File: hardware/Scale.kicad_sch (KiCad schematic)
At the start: 3 parts, among them J1 Load Cell Connector, J4 GPIO, J5 RS232

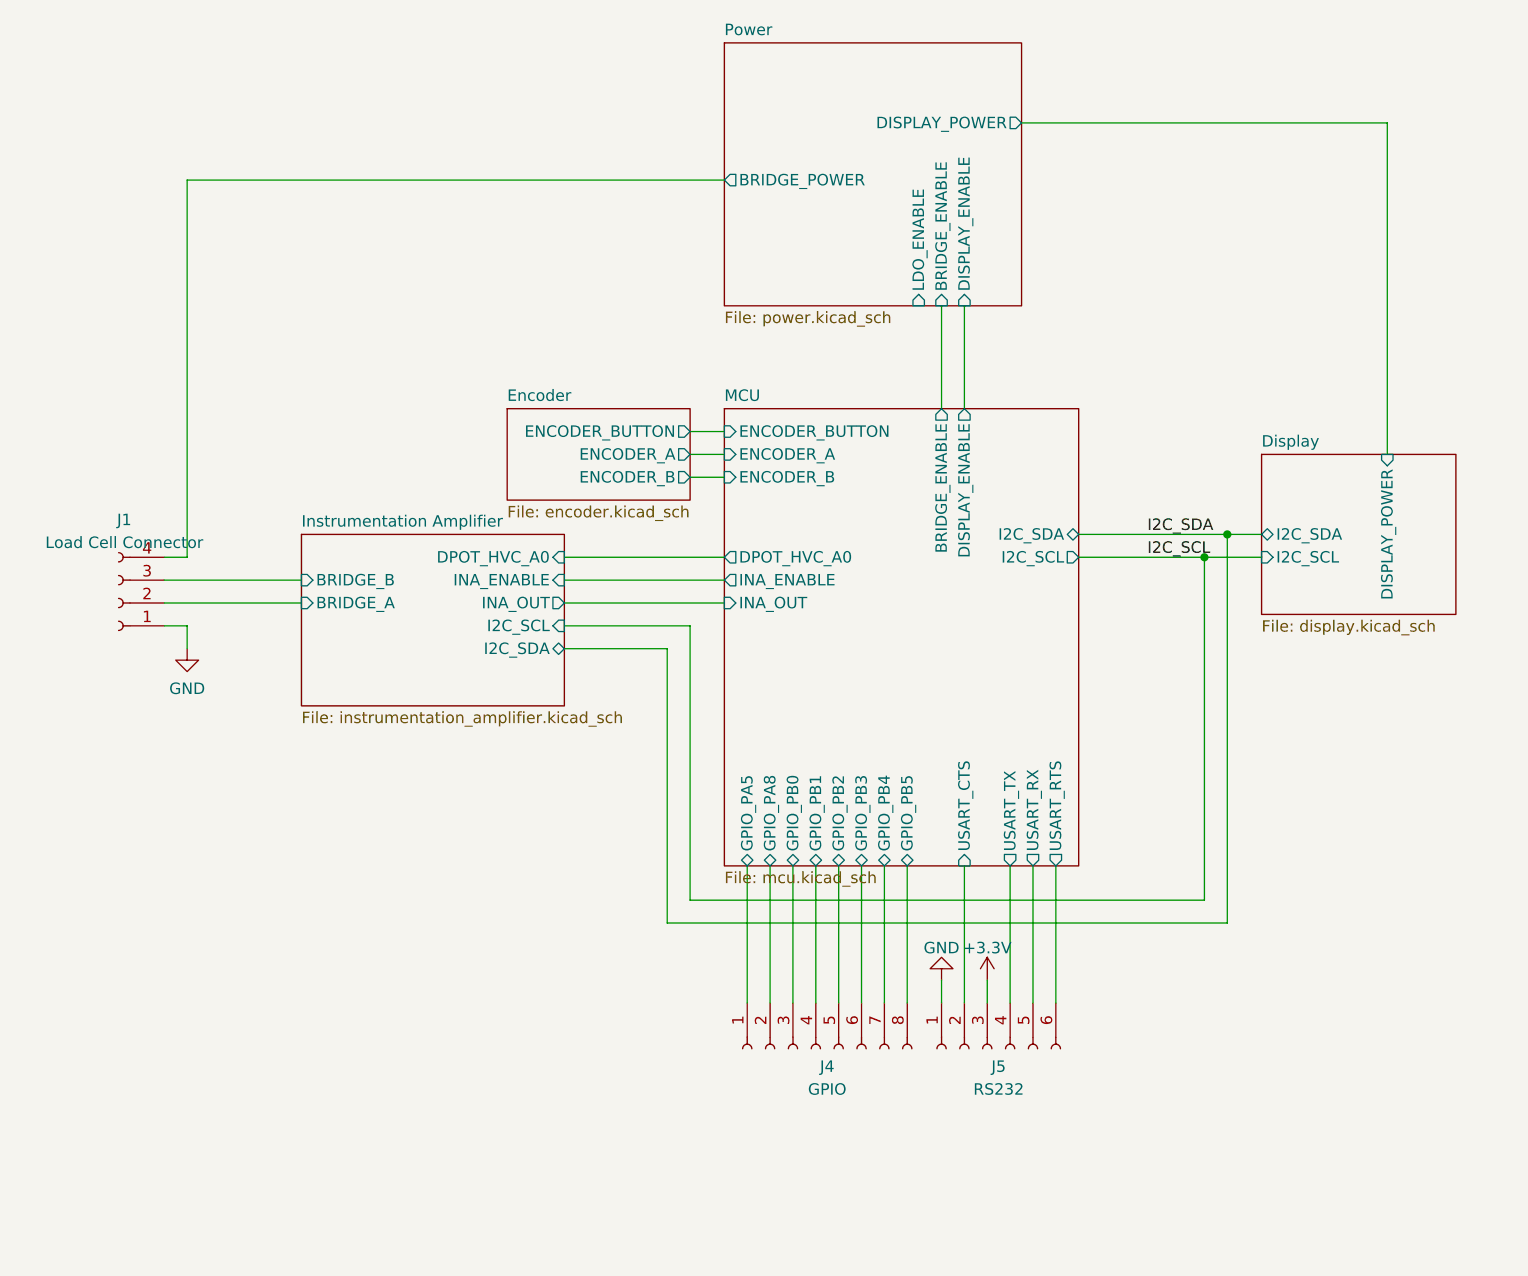
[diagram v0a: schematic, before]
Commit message: Updated schematic according to reference design
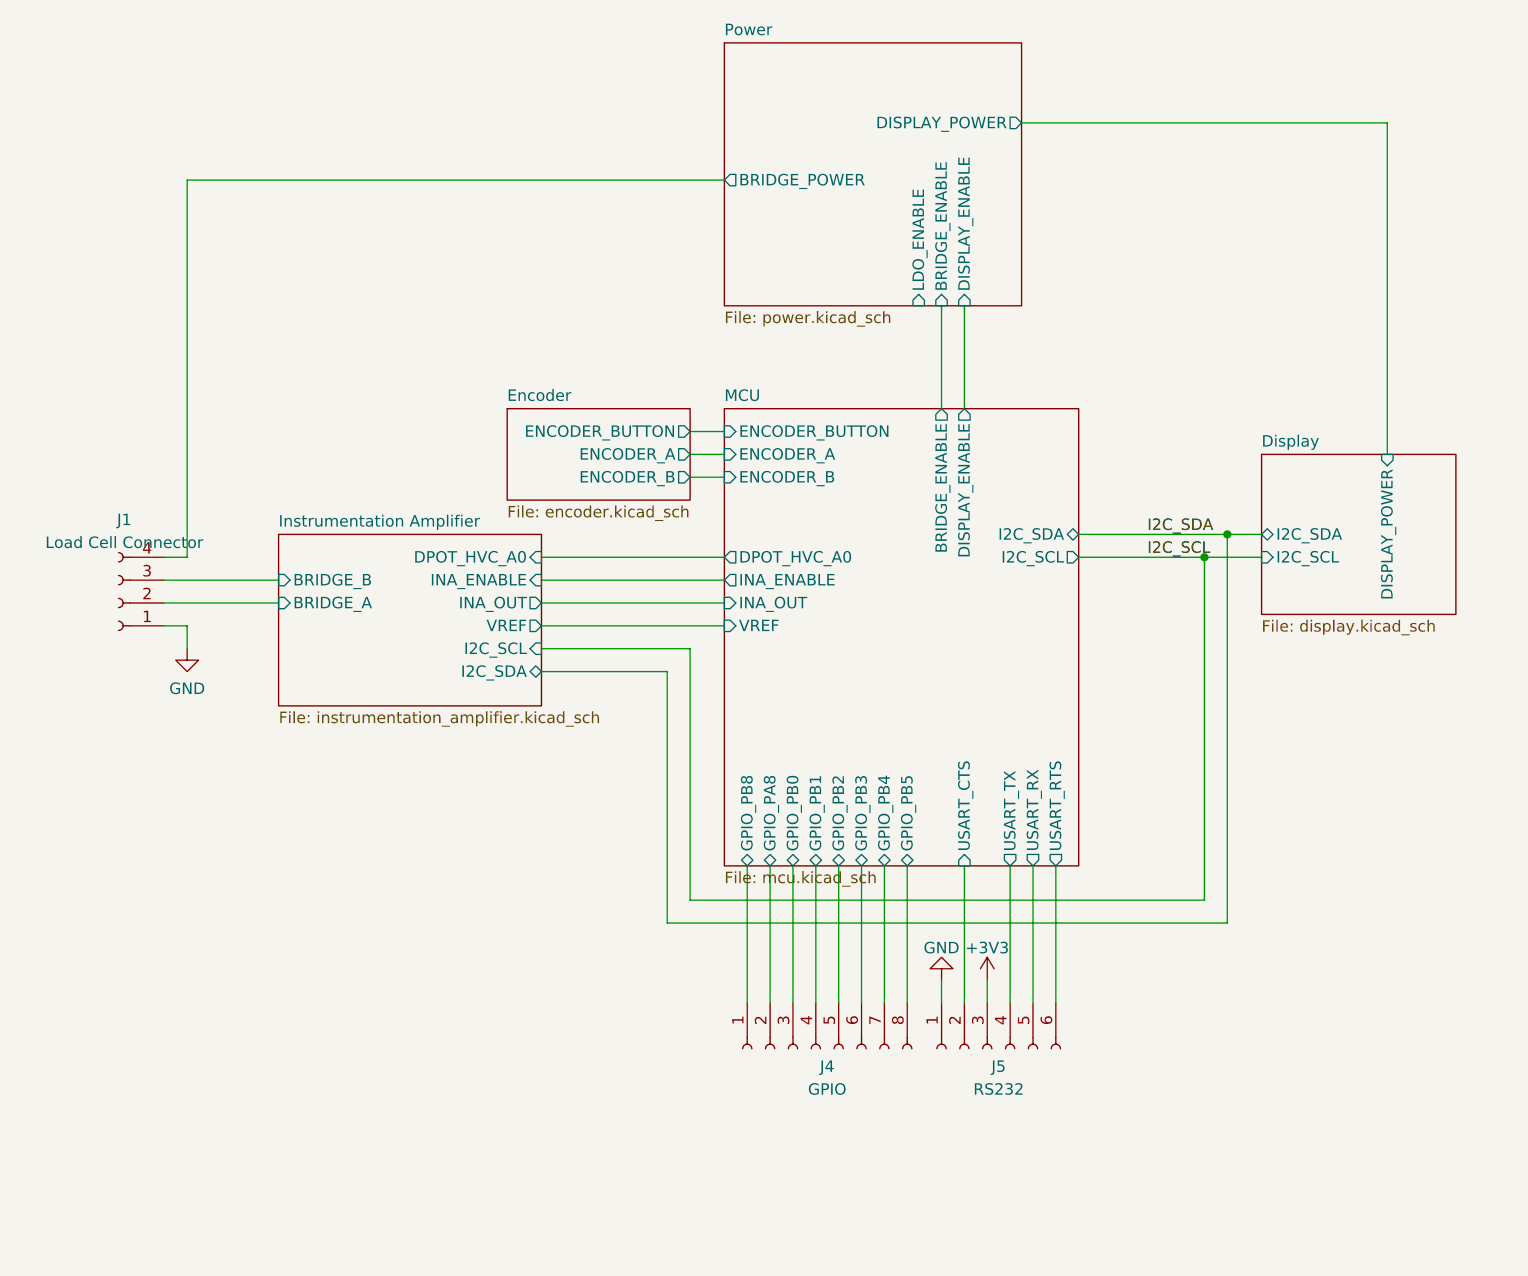
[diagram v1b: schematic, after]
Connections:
- net MCU/GPIO_PA5 renamed MCU/GPIO_PB8
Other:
- sheet Instrumentation Amplifier ports: added VREF; removed none
- sheet MCU ports: added GPIO_PB8, VREF; removed GPIO_PA5

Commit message: Include active filter, ext. ADC, changes to power supply
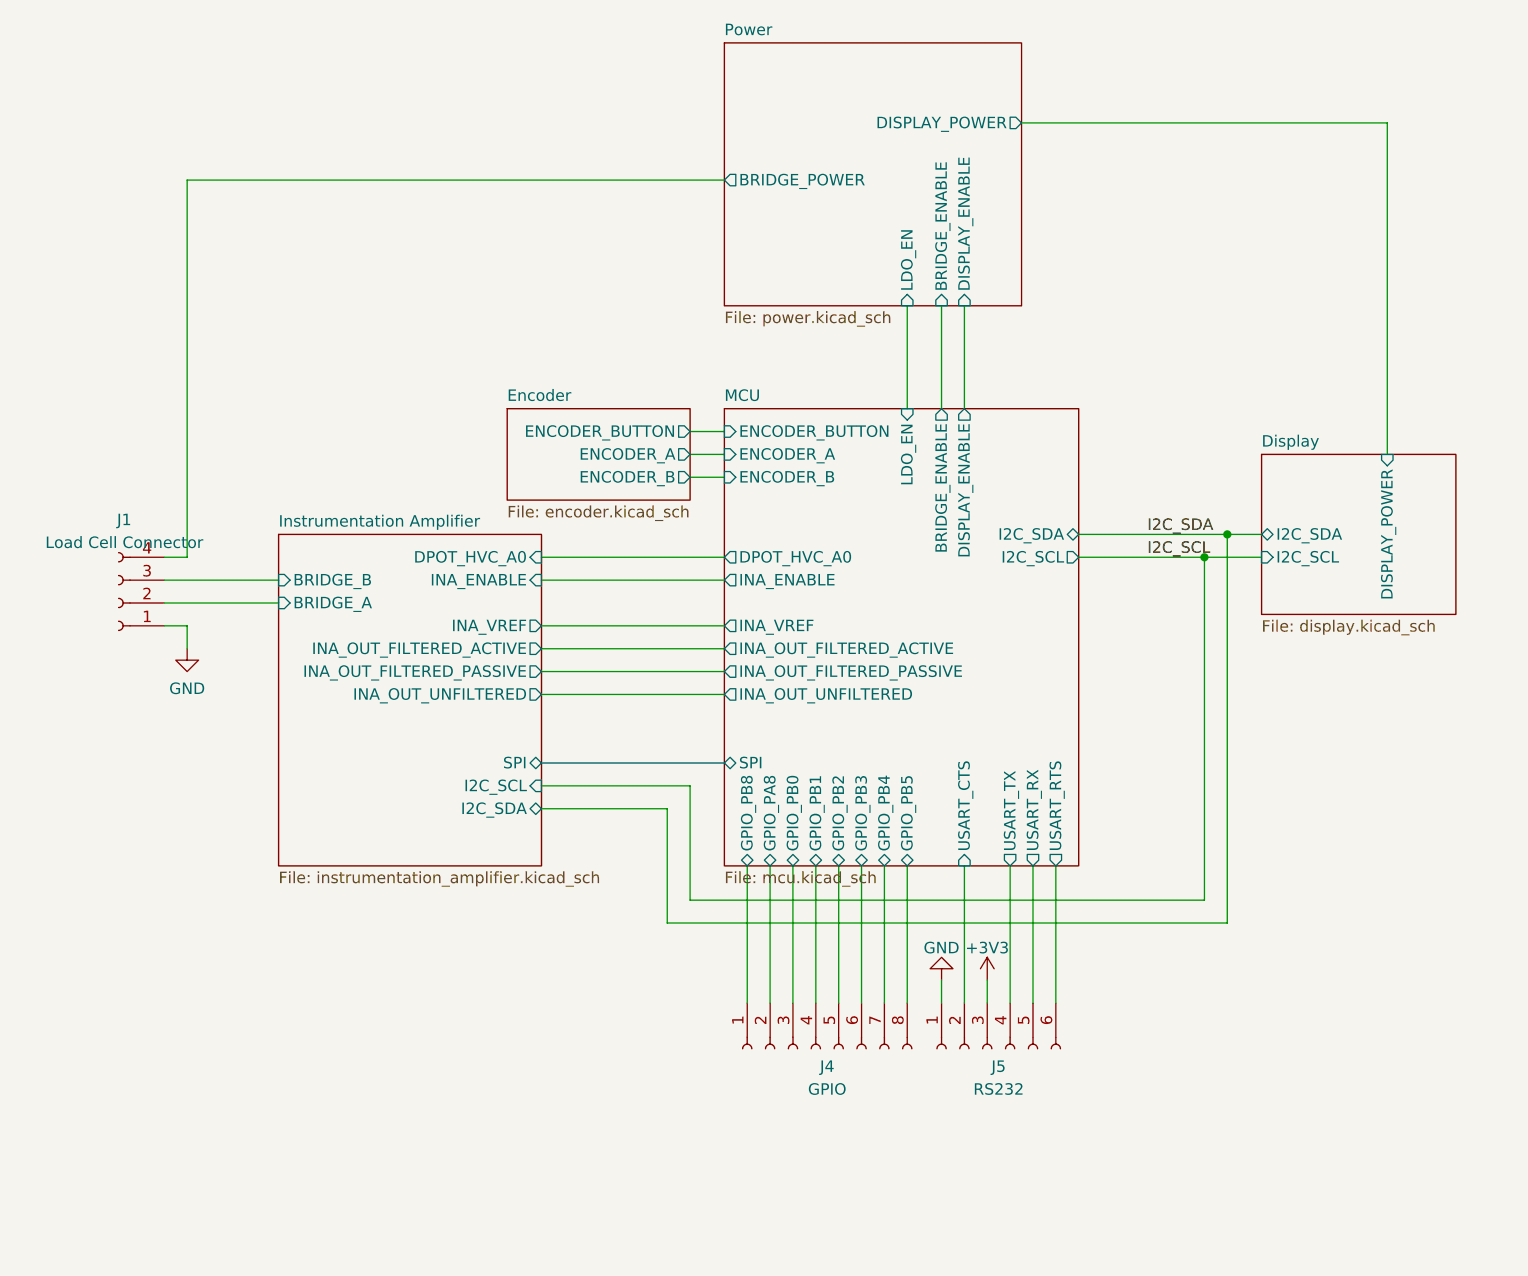
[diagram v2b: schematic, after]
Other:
- sheet Instrumentation Amplifier ports: added INA_OUT_FILTERED_ACTIVE, INA_OUT_FILTERED_PASSIVE, INA_OUT_UNFILTERED, INA_VREF, SPI; removed INA_OUT, VREF
- sheet MCU ports: added INA_OUT_FILTERED_ACTIVE, INA_OUT_FILTERED_PASSIVE, INA_OUT_UNFILTERED, INA_VREF, LDO_EN, SPI; removed INA_OUT, VREF
- sheet Power ports: added LDO_EN; removed LDO_ENABLE
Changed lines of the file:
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@@
-	(wire
-		(pts
-			(xy 99.06 101.6) (xy 119.38 101.6)
-		)
-		(stroke
-			(width 0)
-			(type default)
-		)
-	)
 	(wire
 		(pts
@@
 		)
 	)
+	(bus
+		(pts
+			(xy 99.06 119.38) (xy 119.38 119.38)
+		)
+		(stroke
+			(width 0)
+			(type default)
+		)
+	)
 	(wire
 		(pts
@@
 	(wire
 		(pts
+			(xy 139.7 68.58) (xy 139.7 80.01)
+		)
+		(stroke
+			(width 0)
+			(type default)
+		)
+	)
+	(wire
+		(pts
 			(xy 113.03 137.16) (xy 175.26 137.16)
 		)
@@
 	(wire
 		(pts
-			(xy 99.06 109.22) (xy 113.03 109.22)
+			(xy 99.06 124.46) (xy 113.03 124.46)
+		)
+		(stroke
+			(width 0)
+			(type default)
+		)
+	)
+	(wire
+		(pts
+			(xy 99.06 106.68) (xy 119.38 106.68)
 		)
 		(stroke
@@
 	(wire
 		(pts
+			(xy 99.06 111.76) (xy 119.38 111.76)
+		)
+		(stroke
+			(width 0)
+			(type default)
+		)
+	)
+	(wire
+		(pts
+			(xy 99.06 109.22) (xy 119.38 109.22)
+		)
+		(stroke
+			(width 0)
+			(type default)
+		)
+	)
+	(wire
+		(pts
 			(xy 129.54 130.81) (xy 129.54 146.05)
 		)
@@
 	(wire
 		(pts
-			(xy 113.03 109.22) (xy 113.03 137.16)
+			(xy 113.03 124.46) (xy 113.03 137.16)
 		)
 		(stroke
@@
 	(wire
 		(pts
-			(xy 115.57 106.68) (xy 115.57 134.62)
-		)
-		(stroke
-			(width 0)
-			(type default)
-		)
-	)
-	(wire
-		(pts
-			(xy 99.06 106.68) (xy 115.57 106.68)
+			(xy 115.57 121.92) (xy 115.57 134.62)
+		)
+		(stroke
+			(width 0)
+			(type default)
+		)
+	)
+	(wire
+		(pts
+			(xy 99.06 121.92) (xy 115.57 121.92)
 		)
 		(stroke
@@
 			)
 		)
-		(pin "LDO_ENABLE" input
-			(at 140.97 68.58 270)
+		(pin "LDO_EN" input
+			(at 139.7 68.58 270)
 			(effects
 				(font
@@
 	(sheet
 		(at 69.85 93.98)
-		(size 29.21 19.05)
+		(size 29.21 36.83)
 		(exclude_from_sim no)
 		(in_bom yes)
@@
 		)
 		(property "Sheetfile" "instrumentation_amplifier.kicad_sch"
-			(at 69.85 113.6146 0)
+			(at 69.85 131.3946 0)
 			(effects
 				(font
@@
 				)
 				(justify left top)
-			)
-		)
-		(pin "INA_OUT" output
-			(at 99.06 101.6 0)
-			(effects
-				(font
-					(size 1.27 1.27)
-				)
-				(justify right)
 			)
 		)
@@
 		)
 		(pin "I2C_SCL" input
+			(at 99.06 121.92 0)
+			(effects
+				(font
+					(size 1.27 1.27)
+				)
+				(justify right)
+			)
+		)
+		(pin "I2C_SDA" bidirectional
+			(at 99.06 124.46 0)
+			(effects
+				(font
+					(size 1.27 1.27)
+				)
+				(justify right)
+			)
+		)
+		(pin "SPI" bidirectional
+			(at 99.06 119.38 0)
+			(effects
+				(font
+					(size 1.27 1.27)
+				)
+				(justify right)
+			)
+		)
+		(pin "INA_OUT_FILTERED_ACTIVE" output
 			(at 99.06 106.68 0)
 			(effects
@@
 			)
 		)
-		(pin "I2C_SDA" bidirectional
+		(pin "INA_OUT_FILTERED_PASSIVE" output
 			(at 99.06 109.22 0)
 			(effects
@@
 			)
 		)
-		(pin "VREF" output
+		(pin "INA_OUT_UNFILTERED" output
+			(at 99.06 111.76 0)
+			(effects
+				(font
+					(size 1.27 1.27)
+				)
+				(justify right)
+			)
+		)
+		(pin "INA_VREF" output
 			(at 99.06 104.14 0)
 			(effects
@@
 			)
 		)
-		(pin "INA_OUT" input
-			(at 119.38 101.6 180)
-			(effects
-				(font
-					(size 1.27 1.27)
-				)
-				(justify left)
-			)
-		)
 		(pin "DISPLAY_ENABLE" output
 			(at 146.05 80.01 90)
@@
 			)
 		)
-		(pin "VREF" input
-			(at 119.38 104.14 180)
-			(effects
-				(font
-					(size 1.27 1.27)
-				)
-				(justify left)
-			)
-		)
 		(pin "GPIO_PB8" bidirectional
 			(at 121.92 130.81 270)
@@
 			)
 		)
+		(pin "SPI" bidirectional
+			(at 119.38 119.38 180)
+			(effects
+				(font
+					(size 1.27 1.27)
+				)
+				(justify left)
+			)
+		)
+		(pin "INA_OUT_FILTERED_ACTIVE" output
+			(at 119.38 106.68 180)
+			(effects
+				(font
+					(size 1.27 1.27)
+				)
+				(justify left)
+			)
+		)
+		(pin "INA_OUT_FILTERED_PASSIVE" output
+			(at 119.38 109.22 180)
+			(effects
+				(font
+					(size 1.27 1.27)
+				)
+				(justify left)
+			)
+		)
+		(pin "INA_OUT_UNFILTERED" output
+			(at 119.38 111.76 180)
+			(effects
+				(font
+					(size 1.27 1.27)
+				)
+				(justify left)
+			)
+		)
+		(pin "INA_VREF" output
+			(at 119.38 104.14 180)
+			(effects
+				(font
+					(size 1.27 1.27)
+				)
+				(justify left)
+			)
+		)
+		(pin "LDO_EN" input
+			(at 139.7 80.01 90)
+			(effects
+				(font
+					(size 1.27 1.27)
+				)
+				(justify right)
+			)
+		)

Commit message: Added correct symbol and libraries for ADC
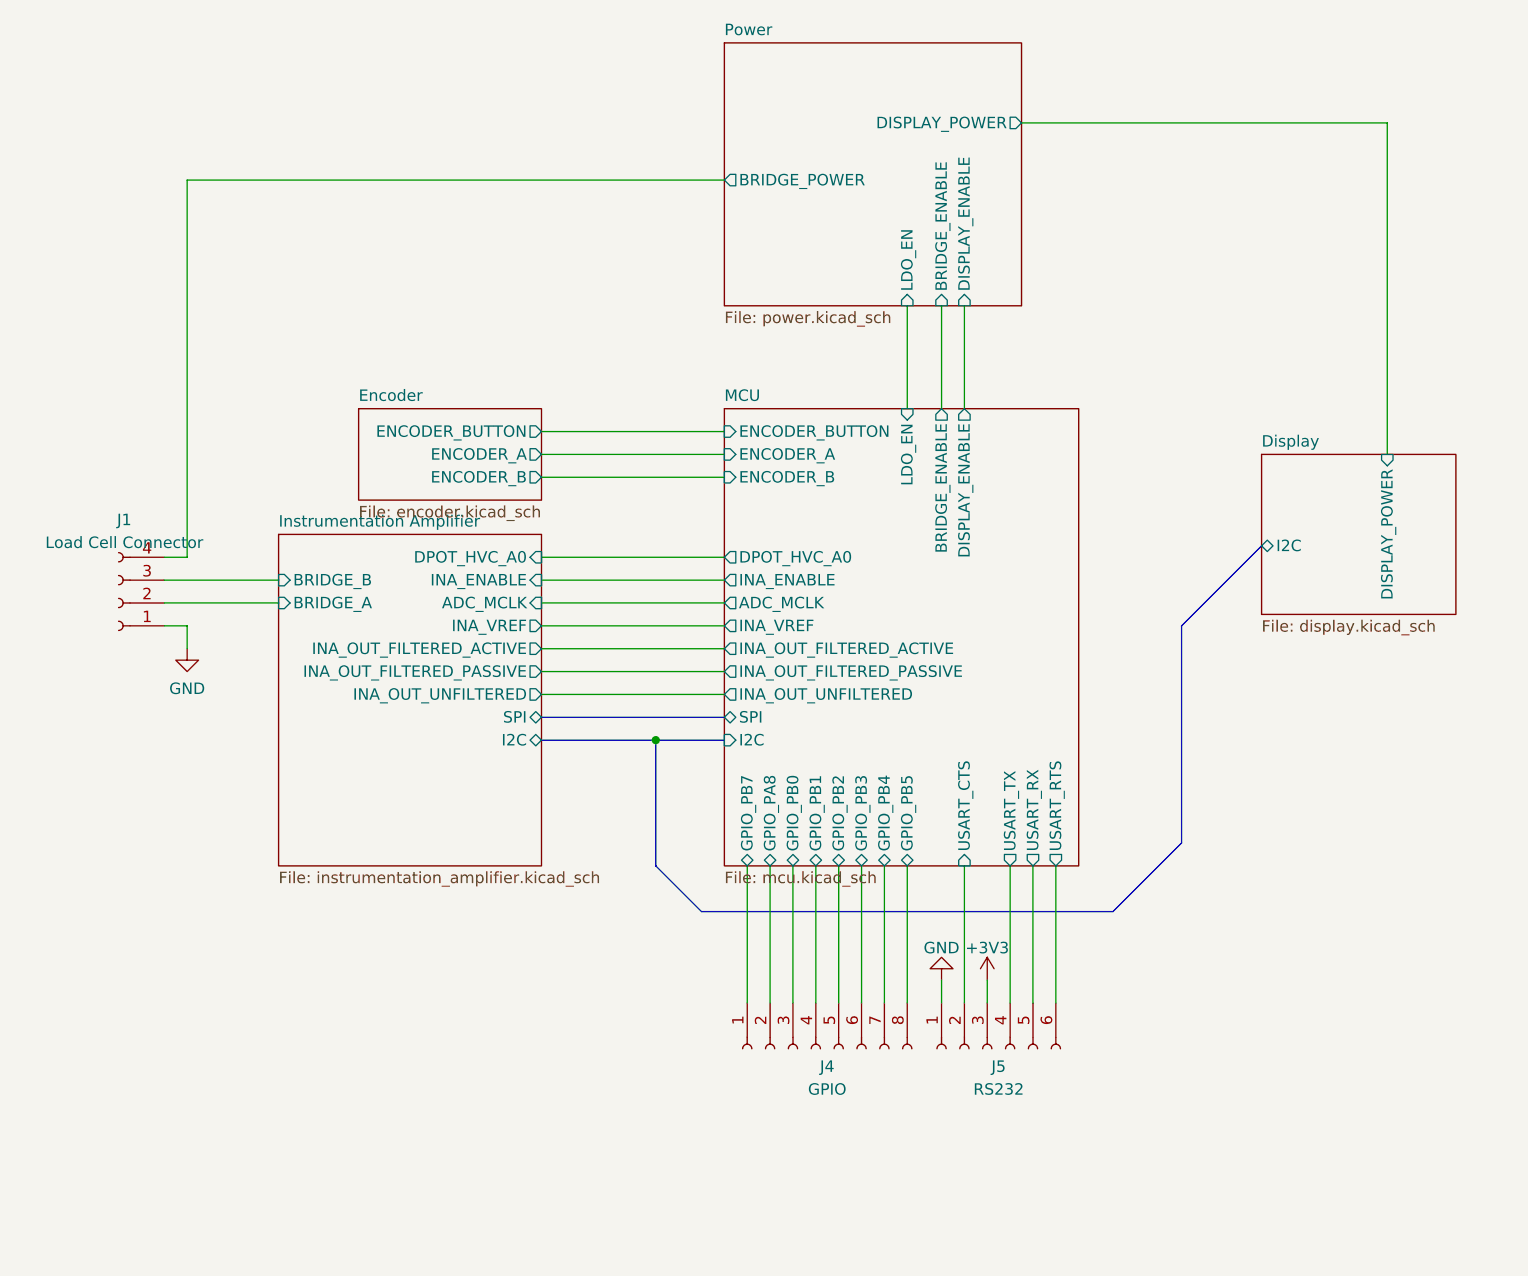
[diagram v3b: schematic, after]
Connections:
- net MCU/GPIO_PB8 renamed MCU/GPIO_PB7
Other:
- sheet Display ports: added I2C; removed I2C_SCL, I2C_SDA
- sheet Instrumentation Amplifier ports: added ADC_MCLK, I2C; removed I2C_SCL, I2C_SDA
- sheet MCU ports: added ADC_MCLK, GPIO_PB7, I2C; removed GPIO_PB8, I2C_SCL, I2C_SDA
